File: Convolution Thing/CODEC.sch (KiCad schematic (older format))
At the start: 7 parts

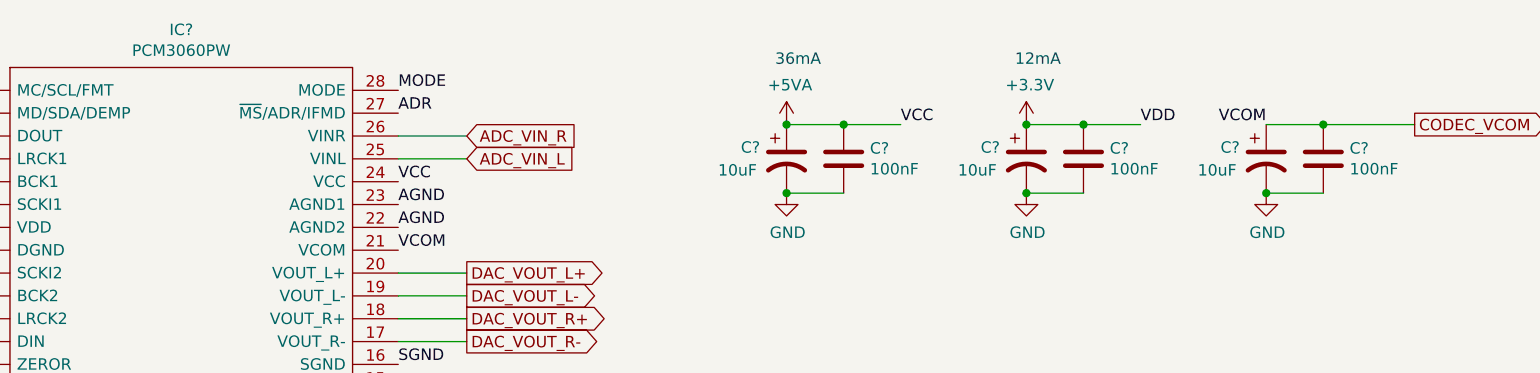
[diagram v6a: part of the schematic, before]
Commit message: Fix some issues, add component references
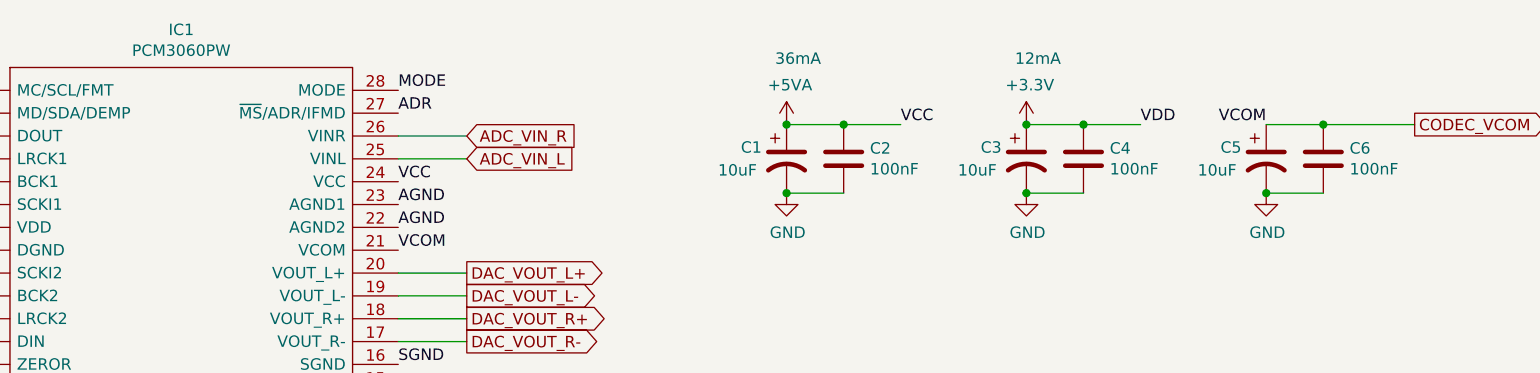
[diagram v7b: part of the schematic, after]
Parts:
- gave numbers to parts that had none: 7
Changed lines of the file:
@@
 VCC
 $Comp
-L power:GND #PWR?
+L power:GND #PWR02
 U 1 1 610989BE
 P 5000 1300
-F 0 "#PWR?" H 5000 1050 50  0001 C CNN
+F 0 "#PWR02" H 5000 1050 50  0001 C CNN
 F 1 "GND" H 5005 1127 50  0000 C CNN
 F 2 "" H 5000 1300 50  0001 C CNN
@@
 $EndComp
 $Comp
-L Device:CP1 C?
+L Device:CP1 C1
 U 1 1 6109A07D
 P 5000 1150
-F 0 "C?" H 4800 1200 50  0000 L CNN
+F 0 "C1" H 4800 1200 50  0000 L CNN
 F 1 "10uF" H 4700 1100 50  0000 L CNN
 F 2 "" H 5000 1150 50  0001 C CNN
@@
 Connection ~ 5250 1000
 $Comp
-L Device:C C?
+L Device:C C2
 U 1 1 610D431D
 P 5250 1150
-F 0 "C?" H 5365 1196 50  0000 L CNN
+F 0 "C2" H 5365 1196 50  0000 L CNN
 F 1 "100nF" H 5365 1105 50  0000 L CNN
 F 2 "" H 5288 1000 50  0001 C CNN
@@
 SGND
 $Comp
-L power:GND #PWR?
+L power:GND #PWR06
 U 1 1 610DA6F6
 P 8750 1250
-F 0 "#PWR?" H 8750 1000 50  0001 C CNN
+F 0 "#PWR06" H 8750 1000 50  0001 C CNN
 F 1 "GND" H 8755 1077 50  0000 C CNN
 F 2 "" H 8750 1250 50  0001 C CNN
@@
 VDD
 $Comp
-L power:+3.3V #PWR?
+L power:+3.3V #PWR03
 U 1 1 610DECC5
 P 6050 1000
-F 0 "#PWR?" H 6050 850 50  0001 C CNN
+F 0 "#PWR03" H 6050 850 50  0001 C CNN
 F 1 "+3.3V" H 6065 1173 50  0000 C CNN
 F 2 "" H 6050 1000 50  0001 C CNN
@@
 $EndComp
 $Comp
-L power:GND #PWR?
+L power:GND #PWR04
 U 1 1 610DECCB
 P 6050 1300
-F 0 "#PWR?" H 6050 1050 50  0001 C CNN
+F 0 "#PWR04" H 6050 1050 50  0001 C CNN
 F 1 "GND" H 6055 1127 50  0000 C CNN
 F 2 "" H 6050 1300 50  0001 C CNN
@@
 $EndComp
 $Comp
-L Device:CP1 C?
+L Device:CP1 C3
 U 1 1 610DECD1
 P 6050 1150
-F 0 "C?" H 5850 1200 50  0000 L CNN
+F 0 "C3" H 5850 1200 50  0000 L CNN
 F 1 "10uF" H 5750 1100 50  0000 L CNN
 F 2 "" H 6050 1150 50  0001 C CNN
@@
 Connection ~ 6050 1000
 $Comp
-L Device:C C?
+L Device:C C4
 U 1 1 610DECDB
 P 6300 1150
-F 0 "C?" H 6415 1196 50  0000 L CNN
+F 0 "C4" H 6415 1196 50  0000 L CNN
 F 1 "100nF" H 6415 1105 50  0000 L CNN
 F 2 "" H 6338 1000 50  0001 C CNN
@@
 Connection ~ 6050 1300
 $Comp
-L power:+5VA #PWR?
+L power:+5VA #PWR01
 U 1 1 610E013F
 P 5000 1000
-F 0 "#PWR?" H 5000 850 50  0001 C CNN
+F 0 "#PWR01" H 5000 850 50  0001 C CNN
 F 1 "+5VA" H 5015 1173 50  0000 C CNN
 F 2 "" H 5000 1000 50  0001 C CNN
@@
 VCOM
 $Comp
-L Device:CP1 C?
+L Device:CP1 C5
 U 1 1 610E6A81
 P 7100 1150
-F 0 "C?" H 6900 1200 50  0000 L CNN
+F 0 "C5" H 6900 1200 50  0000 L CNN
 F 1 "10uF" H 6800 1100 50  0000 L CNN
 F 2 "" H 7100 1150 50  0001 C CNN
@@
 $EndComp
 $Comp
-L Device:C C?
+L Device:C C6
 U 1 1 610E6A87
 P 7350 1150
-F 0 "C?" H 7465 1196 50  0000 L CNN
+F 0 "C6" H 7465 1196 50  0000 L CNN
 F 1 "100nF" H 7465 1105 50  0000 L CNN
 F 2 "" H 7388 1000 50  0001 C CNN
@@
 Connection ~ 7100 1300
 $Comp
-L power:GND #PWR?
+L power:GND #PWR05
 U 1 1 610E6A7B
 P 7100 1300
-F 0 "#PWR?" H 7100 1050 50  0001 C CNN
+F 0 "#PWR05" H 7100 1050 50  0001 C CNN
 F 1 "GND" H 7105 1127 50  0000 C CNN
 F 2 "" H 7100 1300 50  0001 C CNN
@@
 MODE
 $Comp
-L power:GND #PWR?
+L power:GND #PWR07
 U 1 1 610EE813
 P 9600 1250
-F 0 "#PWR?" H 9600 1000 50  0001 C CNN
+F 0 "#PWR07" H 9600 1000 50  0001 C CNN
 F 1 "GND" H 9605 1077 50  0000 C CNN
 F 2 "" H 9600 1250 50  0001 C CNN
@@
 I2C Mode
 $Comp
-L SamacSys:PCM3060PW IC?
+L SamacSys:PCM3060PW IC1
 U 1 1 610925E3
 P 1400 850
-F 0 "IC?" H 2350 1115 50  0000 C CNN
+F 0 "IC1" H 2350 1115 50  0000 C CNN
 F 1 "PCM3060PW" H 2350 1024 50  0000 C CNN
 F 2 "SOP65P640X120-28N" H 3150 950 50  0001 L CNN
@@
 ADR
 $Comp
-L power:GND #PWR?
+L power:GND #PWR08
 U 1 1 610FBA07
 P 10200 1250
-F 0 "#PWR?" H 10200 1000 50  0001 C CNN
+F 0 "#PWR08" H 10200 1000 50  0001 C CNN
 F 1 "GND" H 10205 1077 50  0000 C CNN
 F 2 "" H 10200 1250 50  0001 C CNN

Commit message: Started footprint assignment
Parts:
- IC1: footprint SOP65P640X120-28N -> SamacSys:SOP65P640X120-28N
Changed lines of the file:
@@
 F 0 "IC1" H 2350 1115 50  0000 C CNN
 F 1 "PCM3060PW" H 2350 1024 50  0000 C CNN
-F 2 "SOP65P640X120-28N" H 3150 950 50  0001 L CNN
+F 2 "SamacSys:SOP65P640X120-28N" H 3150 950 50  0001 L CNN
 F 3 "http://componentsearchengine.com/Datasheets/1/PCM3060PW.pdf" H 3150 850 50  0001 L CNN
 F 4 "24-bit Asynchronous Stereo Audio Codec with 96/192kHz sampling rate" H 3150 750 50  0001 L CNN "Description"
